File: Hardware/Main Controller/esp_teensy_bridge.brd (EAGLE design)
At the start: 102.8 x 87.9 mm, 42 parts, among them IC1 BQ79600PWRQ1, Q1 SI7611DN-T1-GE3, Q2 SI7611DN-T1-GE3, Q3 SI7611DN-T1-GE3, Q4 SI7611DN-T1-GE3

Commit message: gnd
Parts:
- moved CCOMLN 35.7 mm to (77.2, 53.0)
- moved CCOMLP 28.8 mm to (77.2, 55.2)
- moved CAN1 16.6 mm to (73.7, 38.1)
- moved ESDCOMH 16.0 mm to (71.4, 58.4)
- moved CCOMHP 14.0 mm to (77.2, 58.4)
- moved ESDCOML 12.6 mm to (71.4, 51.4)
- moved CCOMLNG 12.1 mm to (84.5, 46.4)
- moved RCOMLN 12.1 mm to (84.5, 50.8)
- moved RCOMLP 12.1 mm to (81.3, 25.4)
- moved TME1205S 12.1 mm to (59.1, 21.0)
- moved CCOMHN 12.1 mm to (87.0, 21.6)
- moved CCOMHNG 12.1 mm to (85.1, 11.4)
- moved CCOMHPG 12.1 mm to (92.1, 14.6)
- moved CCOMLPG 12.1 mm to (91.4, 19.7)
- moved RCOMH 12.1 mm to (86.4, 17.1)
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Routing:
- net GND: track 96.8 -> 1.64 mm, vias 4 -> 3
- net 5V: track 102.3 -> 128.0 mm
- net N$8: track 0.00 -> 17.3 mm
- net N$7: track 0.00 -> 15.7 mm
- net TX_ESP: track 1.69 -> 0.00 mm
- added copper zone on layer 1, net GND
- added copper zone on layer 16, net GND

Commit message: connected some stuff
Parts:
- moved C4 28.9 mm to (79.4, 36.2)
- moved RCOMHP 25.4 mm to (88.6, 21.0), turned to 1.8 degrees
- moved C3 24.4 mm to (81.3, 29.2)
- moved C1 16.2 mm to (63.5, 23.8)
- moved CCOMHN 14.1 mm to (98.4, 29.8), turned to 180 degrees
- moved TME1205S 10.8 mm to (58.4, 31.8)
- moved COMH 10.5 mm to (98.4, 41.3)
- moved CCOMLPG 9.96 mm to (100.6, 23.5)
- moved C2 9.94 mm to (63.5, 21.0)
- moved R8 8.98 mm to (72.4, 28.6)
- moved RCOMHN 8.95 mm to (85.4, 7.30)
- moved COML 8.52 mm to (97.8, 55.2)
- moved CCOMHNG 8.52 mm to (92.7, 7.62)
- moved CCOMHPG 8.16 mm to (100.0, 12.7)
- moved RCOMH 6.70 mm to (93.0, 16.5)
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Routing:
- net MISO: track 0.00 -> 72.0 mm, vias 0 -> 4
- net MOSI: track 0.00 -> 69.5 mm, vias 0 -> 2
- net CS0: track 0.00 -> 68.3 mm, vias 0 -> 2
- net SCK: track 51.2 -> 88.7 mm, vias 0 -> 3
- net CS1: track 0.00 -> 27.7 mm
- net VCC: track 84.1 -> 109.0 mm
- net 5V: track 128.0 -> 139.9 mm
- net VIO: track 0.00 -> 9.56 mm
- net N$1: track 0.00 -> 8.51 mm
- net N$8: track 17.3 -> 18.9 mm
- net N$7: track 15.7 -> 17.3 mm

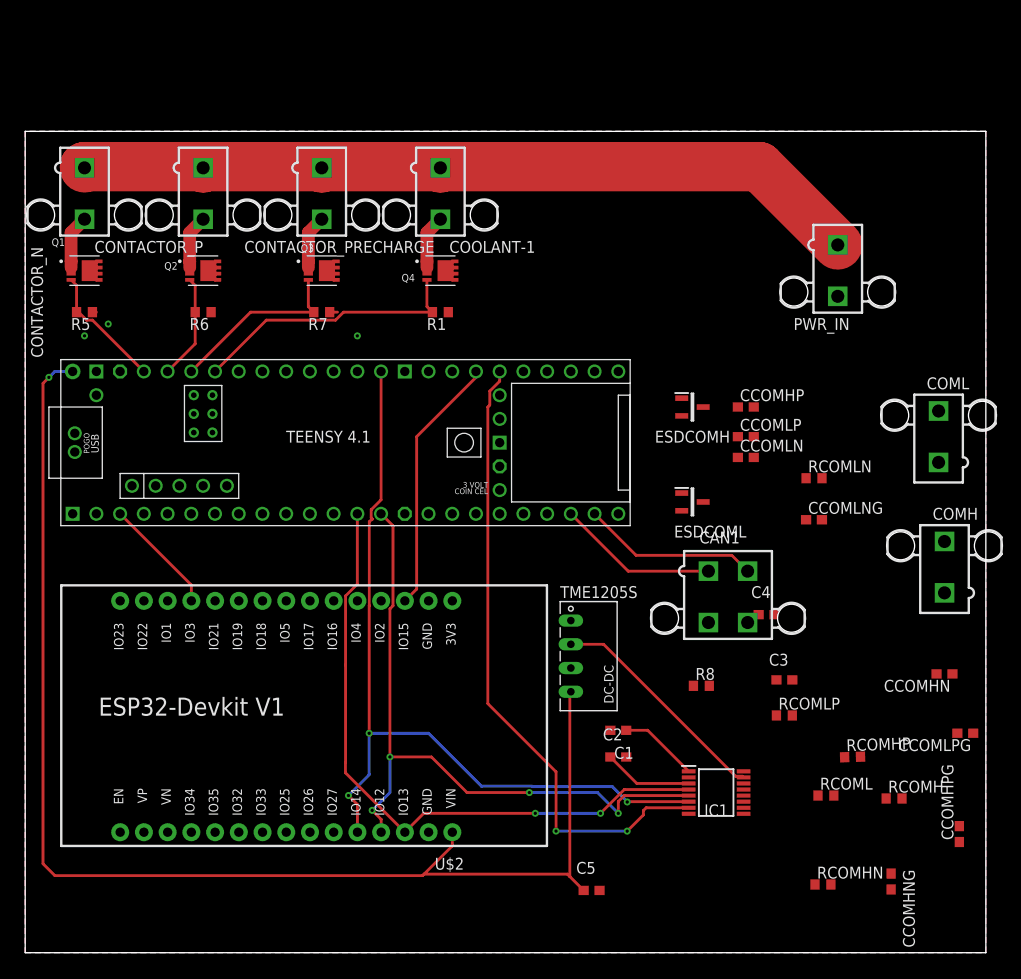
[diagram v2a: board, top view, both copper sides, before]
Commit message: Mainboard routing
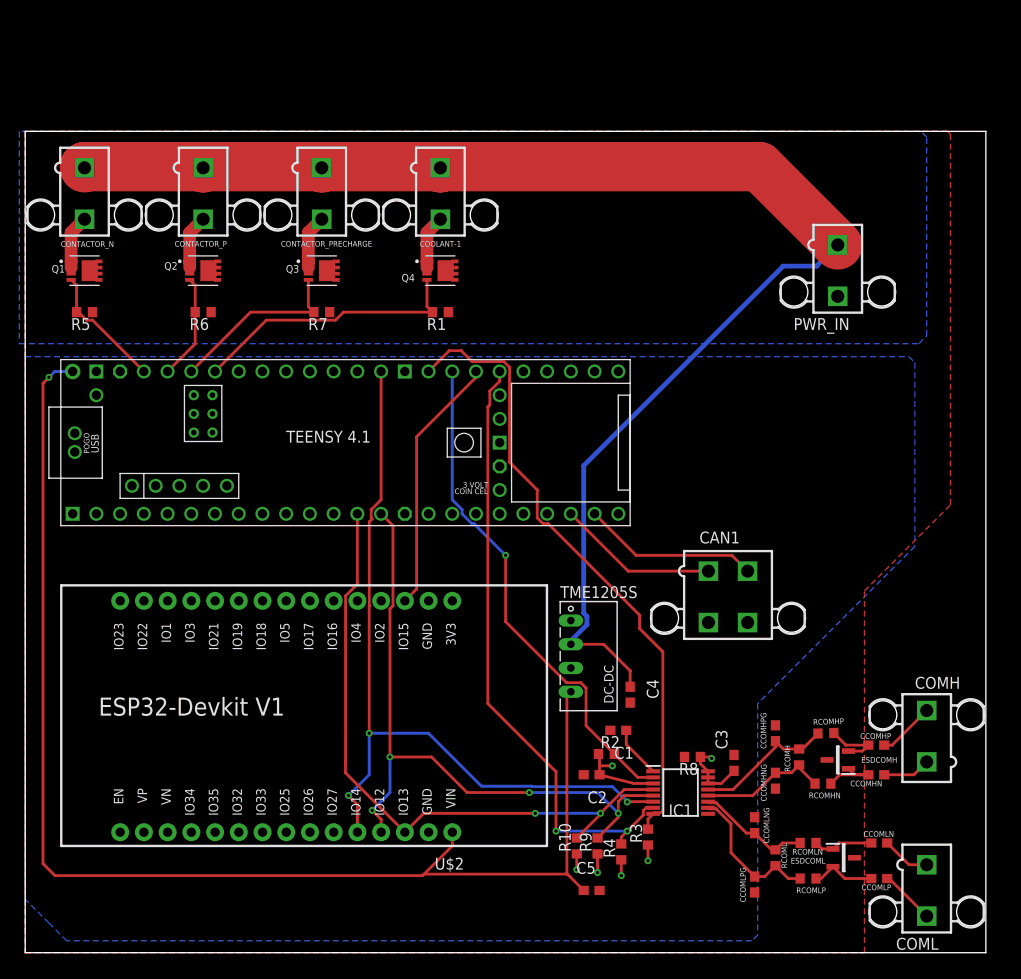
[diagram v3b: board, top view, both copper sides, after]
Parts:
- added R10, R4, R9: 10k, rcl:R0603
- added R2, R3: 100k, rcl:R0603
- moved CCOMLP 49.4 mm to (91.4, 7.94), turned to 180 degrees
- moved COML 48.6 mm to (96.5, 6.67), turned to 180 degrees
- moved CCOMLN 43.7 mm to (91.4, 11.7), turned to 180 degrees
- moved ESDCOML 41.4 mm to (87.6, 10.2)
- moved ESDCOMH 40.9 mm to (87.0, 20.6), turned to 180 degrees
- moved RCOMLN 39.1 mm to (83.8, 11.7), turned to 180 degrees
- moved CCOMHP 38.8 mm to (91.1, 22.2), turned to 180 degrees
- moved CCOMLNG 33.3 mm to (78.1, 13.7), turned to 270 degrees
- moved CCOMLPG 27.8 mm to (78.1, 7.30), turned to 90 degrees
- moved CCOMHPG 22.5 mm to (80.3, 23.5), turned to 270 degrees
- moved COMH 18.2 mm to (96.5, 23.2)
- moved RCOMLP 17.6 mm to (83.8, 7.94), turned to 180 degrees
- moved C4 16.9 mm to (64.8, 27.6), turned to 270 degrees
- moved CCOMHNG 16.4 mm to (80.3, 18.4), turned to 90 degrees
- moved CCOMHN 13.0 mm to (91.1, 19.1)
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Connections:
- removed net CS2: U$3.40-A16/CS1
- removed net GNDN: CCOMHNG.1, CCOMHPG.1, CCOMLNG.1, CCOMLPG.1
- removed net N$3: C3.2, IC1.14
- removed net N$4: IC1.16, R8.1
- removed net VIO: C2.1, IC1.3
- new net NFAULT: IC1.2, R2.2, U$3.40-A16/CS1
- new net SPI_RDY: IC1.8, R3.2, U$3.41-A17/MISO1
- net 5V: now also C2.1, C3.2, IC1.14, IC1.15, IC1.16, IC1.3, R10.1, R2.1, R3.1, R4.1, R8.1, R9.1
- net CS0: now also R4.2
- net GND: now also CCOMHNG.1, CCOMHPG.1, CCOMLNG.1, CCOMLPG.1; no longer IC1.2, IC1.8
- net MISO: now also R9.2
- net MOSI: now also R10.2
- net VCC: no longer IC1.15
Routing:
- net SPI_RDY: track 0.00 -> 68.0 mm
- net NFAULT: track 0.00 -> 54.4 mm, vias 0 -> 1
- net VCC: track 109.0 -> 150.8 mm
- net 5V: track 139.9 -> 164.2 mm, vias 1 -> 7
- net COMLP: track 0.00 -> 15.8 mm
- net COMHP: track 0.00 -> 15.3 mm
- net COMHN: track 0.00 -> 13.8 mm
- net COMLN: track 0.00 -> 12.3 mm
- net RX_ESP: track 12.1 -> 0.00 mm
- net VIO: track 9.56 -> 0.00 mm
- net N$10: track 0.00 -> 6.97 mm
- net N$16: track 0.00 -> 6.80 mm
- net N$15: track 0.00 -> 6.63 mm
- net N$11: track 0.00 -> 6.45 mm
- net COMHP_ISO: track 0.00 -> 6.08 mm
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- added copper zone on layer 16, net 5V
- added copper zone on layer 16, net VCC
- removed copper zone on layer 16, net GND

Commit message: design review changes
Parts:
- moved CAN1 22.9 mm to (87.9, 57.1)
- moved C3 11.0 mm to (74.0, 31.1)
- moved U$2 10.9 mm to (33.7, 25.4), turned to 0 degrees
- moved ESDCOMH 10.0 mm to (83.8, 30.2)
- moved RCOMH 10.0 mm to (79.7, 30.5)
- moved CCOMHNG 10.0 mm to (77.2, 27.9)
- moved CCOMHPG 10.0 mm to (77.2, 33.0)
- moved COMH 10.0 mm to (93.3, 32.7)
- moved RCOMHP 10.0 mm to (82.5, 33.0)
- moved CCOMHN 10.0 mm to (87.9, 28.6)
- moved CCOMHP 10.0 mm to (87.9, 31.8)
- moved RCOMHN 10.0 mm to (82.2, 27.6)
- moved CCOMLN 7.96 mm to (88.3, 19.1)
- moved CCOMLP 7.96 mm to (88.3, 15.2)
- moved CCOMLPG 7.96 mm to (74.9, 14.6)
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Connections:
- net RX_ESP: now also U$2.12
- net TX_ESP: now also U$2.13
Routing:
- net TX_ESP: track 0.00 -> 68.1 mm, vias 0 -> 2
- net RX_ESP: track 0.00 -> 61.7 mm, vias 0 -> 2
- net CS1: track 27.7 -> 68.9 mm, vias 0 -> 1
- net N$8: track 18.9 -> 37.5 mm
- net N$7: track 17.3 -> 35.8 mm
- net MOSI: track 69.4 -> 84.2 mm
- net MISO: track 71.7 -> 80.5 mm, vias 4 -> 2
- net COOLANT_CTRL: track 29.6 -> 37.7 mm
- net COMHP: track 15.3 -> 23.4 mm
- net VCC: track 150.8 -> 143.0 mm
- net CONTACTORPRECHARGE_CTRL: track 19.4 -> 26.9 mm
- net COMHN: track 13.8 -> 20.7 mm
- net CONTACTORP_CTRL: track 11.3 -> 16.8 mm
- net COMLP: track 15.8 -> 11.1 mm
- net 5V: track 164.2 -> 168.8 mm, vias 7 -> 6
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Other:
- board size 102.8 x 87.9 mm -> 99.7 x 88.3 mm
- board text added: "BMS Main Board V1"
- board text added: "Luc Ah-Hot, Joshua Feist, Lance Go, Isaac Kim Jan 2022"
